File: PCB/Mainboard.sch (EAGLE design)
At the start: 23 parts, among them T1 RM2302, T2 RM2302, T3 RM2302

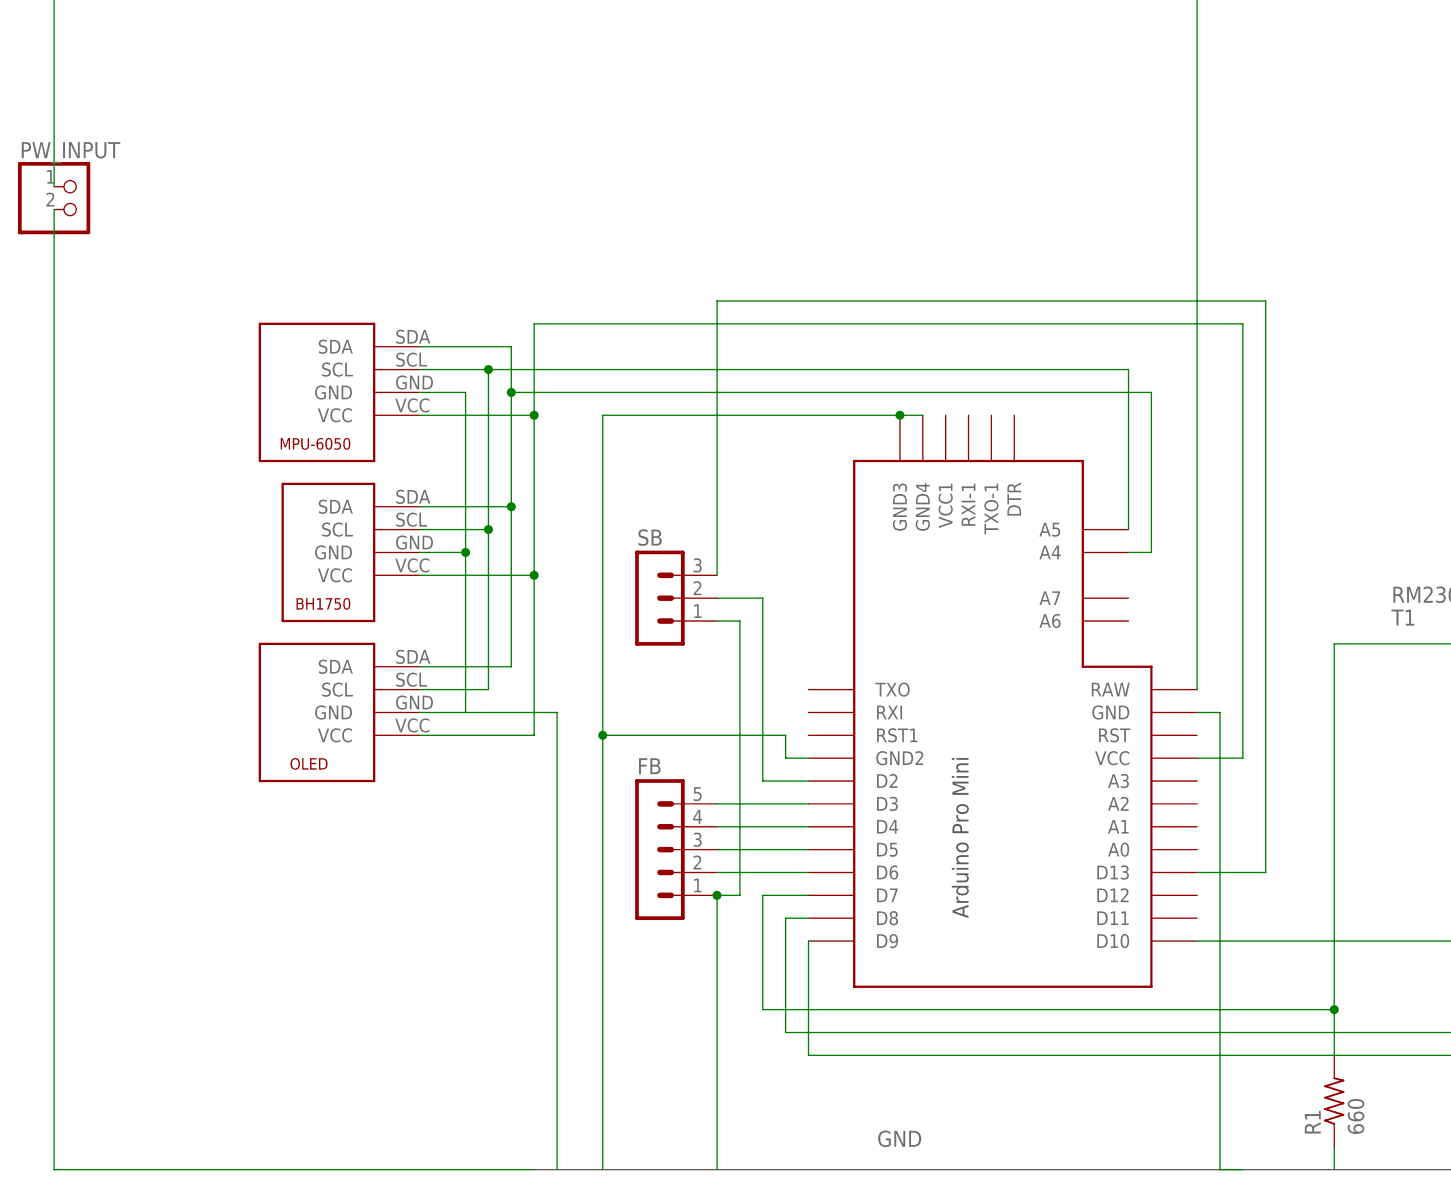
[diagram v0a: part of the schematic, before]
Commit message: Add voltage sense line for battery
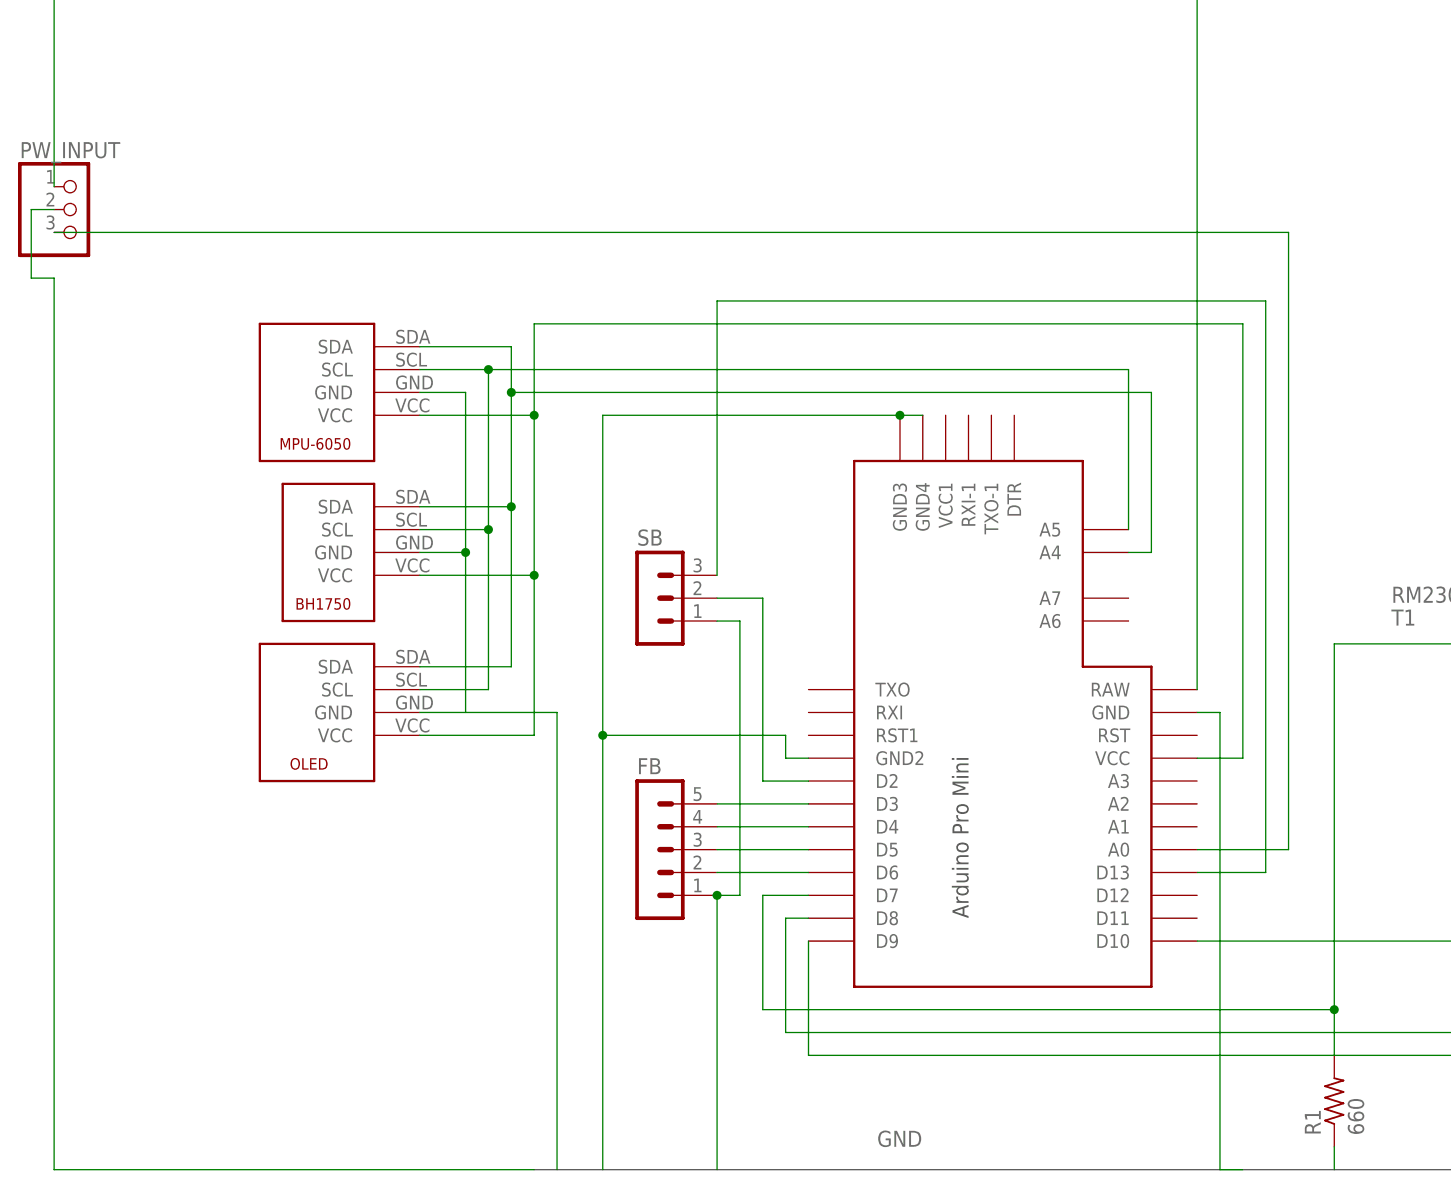
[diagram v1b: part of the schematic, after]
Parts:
- PW_INPUT: device pinhead:PINHD-1X2 -> pinhead:PINHD-1X3
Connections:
- new net BAT_SENSE: PW_INPUT.3, U$7.A0
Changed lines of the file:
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@@
 <part name="U$7" library="Arduino-clone" deviceset="PRO-MINI-2" device=""/>
 <part name="U$1" library="infineon" deviceset="SHUTTER" device=""/>
-<part name="PW_INPUT" library="pinhead" library_urn="urn:adsk.eagle:library:325" deviceset="PINHD-1X2" device="" package3d_urn="urn:adsk.eagle:package:22435/2"/>
+<part name="PW_INPUT" library="pinhead" library_urn="urn:adsk.eagle:library:325" deviceset="PINHD-1X3" device="" package3d_urn="urn:adsk.eagle:package:22458/2"/>
 <part name="MPU6050" library="infineon" deviceset="MPU-6050" device=""/>
 <part name="BH1750" library="infineon" deviceset="BH1750" device=""/>
@@
 <instance part="U$7" gate="G$1" x="71.12" y="22.86"/>
 <instance part="U$1" gate="G$1" x="223.52" y="76.2"/>
-<instance part="PW_INPUT" gate="G$1" x="-33.02" y="88.9"/>
+<instance part="PW_INPUT" gate="A" x="-33.02" y="88.9"/>
 <instance part="MPU6050" gate="G$1" x="-7.62" y="68.58" rot="R180"/>
 <instance part="BH1750" gate="G$1" x="-17.78" y="55.88" rot="R180"/>
@@
 </segment>
 <segment>
-<pinref part="PW_INPUT" gate="G$1" pin="2"/>
-<wire x1="-35.56" y1="88.9" x2="-35.56" y2="-17.78" width="0.1524" layer="91"/>
+<pinref part="PW_INPUT" gate="A" pin="2"/>
+<wire x1="-35.56" y1="88.9" x2="-38.1" y2="88.9" width="0.1524" layer="91"/>
+<wire x1="-38.1" y1="88.9" x2="-38.1" y2="81.28" width="0.1524" layer="91"/>
+<wire x1="-38.1" y1="81.28" x2="-35.56" y2="81.28" width="0.1524" layer="91"/>
+<wire x1="-35.56" y1="81.28" x2="-35.56" y2="-17.78" width="0.1524" layer="91"/>
 <wire x1="-35.56" y1="-17.78" x2="17.78" y2="-17.78" width="0.1524" layer="91"/>
 </segment>
@@
 </segment>
 <segment>
-<pinref part="PW_INPUT" gate="G$1" pin="1"/>
+<pinref part="PW_INPUT" gate="A" pin="1"/>
 <wire x1="-35.56" y1="91.44" x2="-35.56" y2="119.38" width="0.1524" layer="91"/>
 <wire x1="-35.56" y1="119.38" x2="17.78" y2="119.38" width="0.1524" layer="91"/>
@@
 </segment>
 </net>
+<net name="BAT_SENSE" class="0">
+<segment>
+<pinref part="PW_INPUT" gate="A" pin="3"/>
+<wire x1="-35.56" y1="86.36" x2="101.6" y2="86.36" width="0.1524" layer="91"/>
+<wire x1="101.6" y1="86.36" x2="101.6" y2="17.78" width="0.1524" layer="91"/>
+<pinref part="U$7" gate="G$1" pin="A0"/>
+<wire x1="101.6" y1="17.78" x2="91.44" y2="17.78" width="0.1524" layer="91"/>
+</segment>
+</net>
